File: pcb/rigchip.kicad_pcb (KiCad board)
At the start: 2 copper layers, 41 x 51 mm, 34 parts, among them IC1 TSR1, IC2 CHIPv1_0, IC3 SN74LVC1G07, IC4 SN74LVC1G07, J1 POWER, J2 DATA, J3 CONTROL

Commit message: more tweaking
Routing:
- net /PTT: track 20.2 -> 20.9 mm
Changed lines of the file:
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@@
   (general
     (links 73)
-    (no_connects 12)
-    (area 49.924999 48.924999 91.075001 100.075001)
+    (no_connects 0)
+    (area 48.794999 36.645 92.205001 101.625)
     (thickness 1.6)
     (drawings 18)
-    (tracks 349)
+    (tracks 345)
     (zones 0)
     (modules 34)
@@
   )
   (setup
-    (last_trace_width 0.3)
+    (last_trace_width 0.2)
     (user_trace_width 0.2)
     (user_trace_width 0.3)
@@
     (effects (font (size 1.5 1.5) (thickness 0.3)))
   )
+  (segment (start 63 57.46) (end 64.86 57.46) (width 0.3) (layer F.Cu) (net 1))
+  (segment (start 65.6 58.2) (end 65.6 71.1) (width 0.3) (layer F.Cu) (net 1))
+  (segment (start 65.6 71.1) (end 63.6 73.1) (width 0.3) (layer F.Cu) (net 1))
+  (segment (start 64.7 79.8) (end 65.5 79.8) (width 0.3) (layer F.Cu) (net 1))
+  (segment (start 64.86 57.46) (end 65.6 58.2) (width 0.3) (layer F.Cu) (net 1))
+  (segment (start 65.5 75) (end 65.8 75.3) (width 0.3) (layer F.Cu) (net 1))
+  (segment (start 63.6 73.1) (end 63.6 74.6) (width 0.3) (layer F.Cu) (net 1))
+  (segment (start 65.4 76.8) (end 64.8 76.8) (width 0.3) (layer F.Cu) (net 1))
+  (segment (start 63.6 74.6) (end 64 75) (width 0.3) (layer F.Cu) (net 1))
+  (segment (start 64 75) (end 65.5 75) (width 0.3) (layer F.Cu) (net 1))
+  (segment (start 65.8 75.3) (end 65.8 76.4) (width 0.3) (layer F.Cu) (net 1))
+  (segment (start 65.8 76.4) (end 65.4 76.8) (width 0.3) (layer F.Cu) (net 1))
+  (segment (start 64.8 76.8) (end 64.5 77.1) (width 0.3) (layer F.Cu) (net 1))
+  (segment (start 64.5 77.1) (end 64.5 79.6) (width 0.3) (layer F.Cu) (net 1))
+  (segment (start 64.5 79.6) (end 64.7 79.8) (width 0.3) (layer F.Cu) (net 1))
   (segment (start 65.5 79.8) (end 65.525 79.8) (width 0.2) (layer F.Cu) (net 1))
   (segment (start 66.349999 78.975001) (end 68.699999 78.975001) (width 0.2) (layer F.Cu) (net 1))
@@
   (segment (start 68.699999 78.975001) (end 69.475 78.2) (width 0.2) (layer F.Cu) (net 1))
   (segment (start 69.475 78.2) (end 69.5 78.2) (width 0.2) (layer F.Cu) (net 1))
-  (segment (start 64.86 57.46) (end 65.4 58) (width 0.3) (layer F.Cu) (net 1))
-  (segment (start 65.6 71.1) (end 65.6 58.2) (width 0.3) (layer F.Cu) (net 1))
-  (segment (start 64.5 77.1) (end 64.8 76.8) (width 0.3) (layer F.Cu) (net 1))
-  (segment (start 65.4 76.8) (end 65.8 76.4) (width 0.3) (layer F.Cu) (net 1))
-  (segment (start 65.5 79.8) (end 64.7 79.8) (width 0.3) (layer F.Cu) (net 1))
-  (segment (start 65.6 58.2) (end 65.4 58) (width 0.3) (layer F.Cu) (net 1))
-  (segment (start 64.7 79.8) (end 64.5 79.6) (width 0.3) (layer F.Cu) (net 1))
-  (segment (start 64.5 79.6) (end 64.5 77.1) (width 0.3) (layer F.Cu) (net 1))
-  (segment (start 64.8 76.8) (end 65.4 76.8) (width 0.3) (layer F.Cu) (net 1))
-  (segment (start 65.8 76.4) (end 65.8 75.2) (width 0.3) (layer F.Cu) (net 1))
-  (segment (start 65.8 75.2) (end 65.4 74.8) (width 0.3) (layer F.Cu) (net 1))
-  (segment (start 65.4 74.8) (end 63.8 74.8) (width 0.3) (layer F.Cu) (net 1))
-  (segment (start 63.8 74.8) (end 63.6 74.6) (width 0.3) (layer F.Cu) (net 1))
-  (segment (start 63.6 73.1) (end 65.6 71.1) (width 0.3) (layer F.Cu) (net 1))
-  (segment (start 63.6 74.6) (end 63.6 73.1) (width 0.3) (layer F.Cu) (net 1))
-  (segment (start 63 57.46) (end 64.86 57.46) (width 0.3) (layer F.Cu) (net 1))
   (segment (start 69.5 78.2) (end 69.5 76.15) (width 0.3) (layer F.Cu) (net 1))
   (segment (start 69.5 76.15) (end 69.7 75.95) (width 0.3) (layer F.Cu) (net 1))
@@
   (segment (start 80.475 76.05) (end 80.5 76.05) (width 0.2) (layer F.Cu) (net 5))
   (segment (start 80.5 78.2) (end 80.5 76.05) (width 0.3) (layer F.Cu) (net 5))
+  (segment (start 82.5 76.05) (end 81.8 76.05) (width 0.2) (layer F.Cu) (net 6))
+  (segment (start 81.8 76.05) (end 81.5 75.75) (width 0.2) (layer F.Cu) (net 6))
+  (segment (start 86.180009 64.860009) (end 87.03 65.71) (width 0.2) (layer F.Cu) (net 6))
+  (segment (start 81.5 75.75) (end 81.5 72.75) (width 0.2) (layer F.Cu) (net 6))
+  (segment (start 81.5 72.75) (end 81.25 72.5) (width 0.2) (layer F.Cu) (net 6))
+  (segment (start 81.25 72.5) (end 81.25 65.184998) (width 0.2) (layer F.Cu) (net 6))
+  (segment (start 81.25 65.184998) (end 81.574989 64.860009) (width 0.2) (layer F.Cu) (net 6))
+  (segment (start 81.574989 64.860009) (end 86.180009 64.860009) (width 0.2) (layer F.Cu) (net 6))
   (segment (start 87.03 65.71) (end 86.57 65.25) (width 0.2) (layer F.Cu) (net 6))
-  (segment (start 86.57 65.25) (end 85.5 65.25) (width 0.2) (layer F.Cu) (net 6))
-  (segment (start 85.5 65.25) (end 85.110009 64.860009) (width 0.2) (layer F.Cu) (net 6))
-  (segment (start 85.110009 64.860009) (end 81.574989 64.860009) (width 0.2) (layer F.Cu) (net 6))
-  (segment (start 81.574989 64.860009) (end 81.25 65.184998) (width 0.2) (layer F.Cu) (net 6))
-  (segment (start 81.25 65.184998) (end 81.25 72.5) (width 0.2) (layer F.Cu) (net 6))
-  (segment (start 81.25 72.5) (end 81.5 72.75) (width 0.2) (layer F.Cu) (net 6))
-  (segment (start 81.5 72.75) (end 81.5 75.75) (width 0.2) (layer F.Cu) (net 6))
-  (segment (start 81.5 75.75) (end 81.8 76.05) (width 0.2) (layer F.Cu) (net 6))
-  (segment (start 81.8 76.05) (end 82.5 76.05) (width 0.2) (layer F.Cu) (net 6))
   (segment (start 82.475 76.05) (end 82.5 76.05) (width 0.2) (layer F.Cu) (net 6))
   (segment (start 82.5 78.2) (end 82.5 76.05) (width 0.3) (layer F.Cu) (net 6))
@@
   (segment (start 87.03 55.55) (end 86.8 55.55) (width 0.3) (layer F.Cu) (net 81))
   (segment (start 86.98 55.5) (end 87.03 55.55) (width 0.3) (layer F.Cu) (net 81))
-  (segment (start 87.03 53.01) (end 76.99 53.01) (width 0.3) (layer F.Cu) (net 82))
-  (segment (start 76.99 53.01) (end 68.799999 61.200001) (width 0.3) (layer F.Cu) (net 82))
-  (segment (start 68.799999 61.200001) (end 68.799999 72.700001) (width 0.3) (layer F.Cu) (net 82))
-  (segment (start 68.799999 72.700001) (end 68.5 73) (width 0.3) (layer F.Cu) (net 82))
+  (segment (start 87.03 53.01) (end 76.24 53.01) (width 0.3) (layer F.Cu) (net 82))
+  (segment (start 76.24 53.01) (end 68.5 60.75) (width 0.3) (layer F.Cu) (net 82))
+  (segment (start 68.5 60.75) (end 68.5 74.65) (width 0.3) (layer F.Cu) (net 82))
+  (segment (start 68.5 74.65) (end 68.15 75) (width 0.3) (layer F.Cu) (net 82))
   (segment (start 68.15 75) (end 67.3 75) (width 0.3) (layer F.Cu) (net 82))
-  (segment (start 68.5 73) (end 68.5 74.65) (width 0.3) (layer F.Cu) (net 82))
-  (segment (start 68.5 74.65) (end 68.15 75) (width 0.3) (layer F.Cu) (net 82))
   (zone (net 2) (net_name GND) (layer B.Cu) (hatch edge 0.508)
     (connect_pads (clearance 0.3))

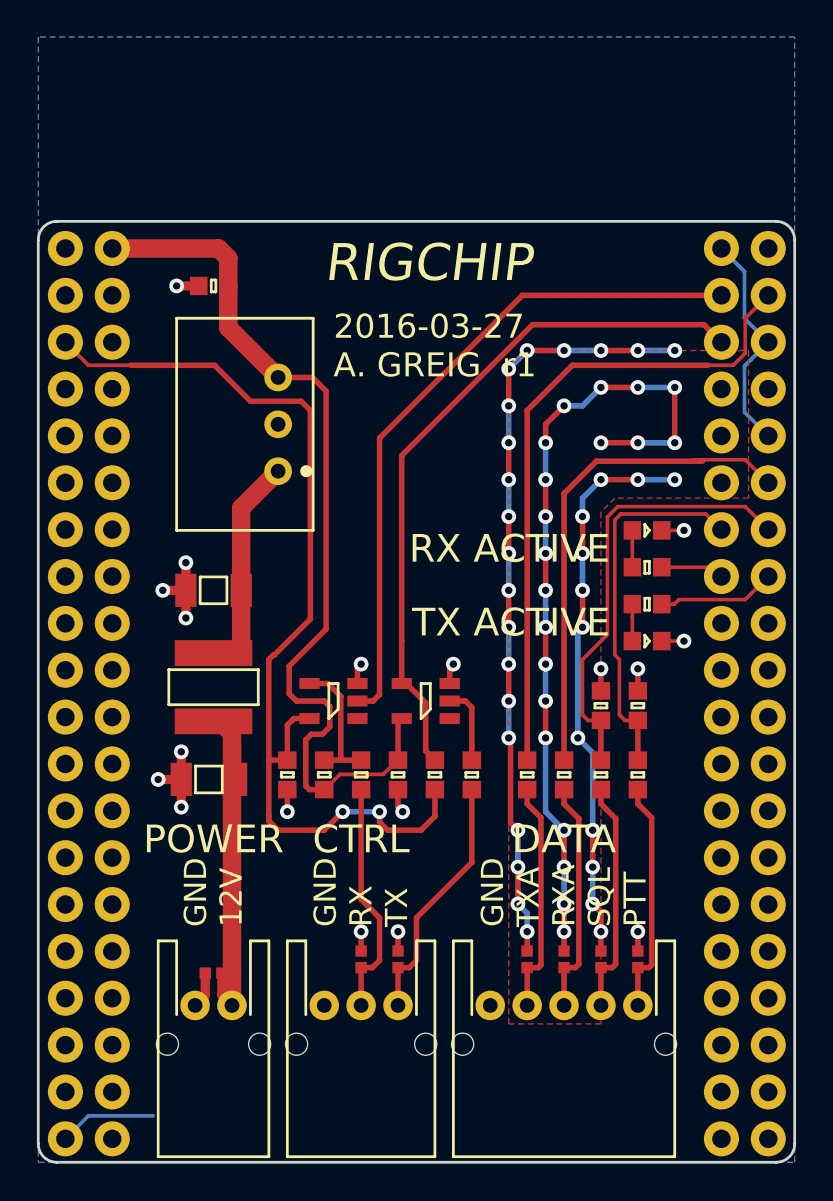
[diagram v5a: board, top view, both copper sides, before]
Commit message: LEDs to sink, driver on PTT, zener+R on SQL, reroute
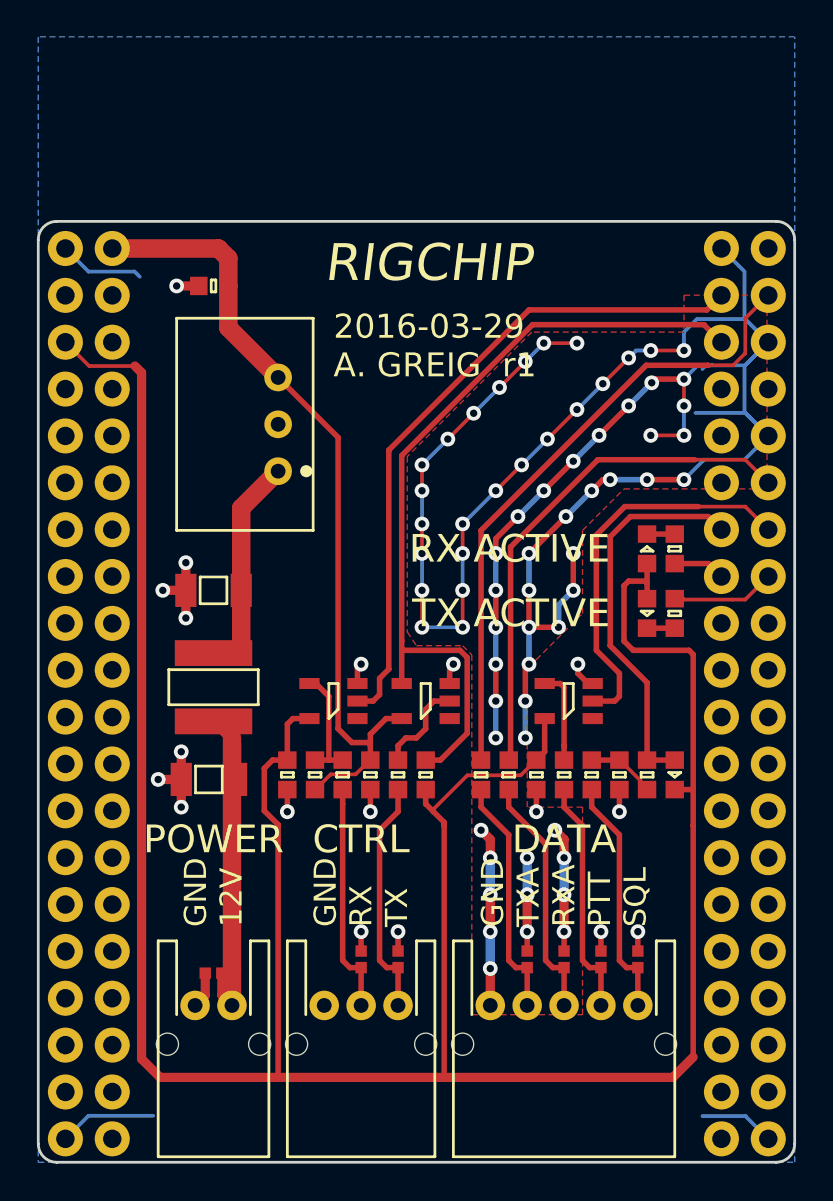
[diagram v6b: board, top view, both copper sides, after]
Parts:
- added D10: ~, agg:0603-LED, F.Cu at (84.5, 79.0)
- added IC5: SN74LVC1G07, agg:SOT-23-5, F.Cu at (78.8, 75.0)
- added R5: 10k, agg:0603, F.Cu at (83.0, 79.0)
- moved C5 6.66 mm to (77.0, 79.0), turned to 270 degrees
- moved L6 4.00 mm to (69.5, 79.0)
- moved C4 3.88 mm to (81.5, 79.0), turned to 270 degrees
- moved L4 3.00 mm to (75.5, 79.0)
- moved L2 2.50 mm to (80.0, 79.0)
- moved L5 2.50 mm to (74.0, 79.0)
- moved L3 2.00 mm to (78.5, 79.0)
- moved R1 1.80 mm to (84.5, 66.8), turned to 90 degrees
- moved R2 1.58 mm to (84.5, 70.2), turned to 270 degrees
- moved C7 1.50 mm to (68.0, 79.0)
- moved D9 1.50 mm to (83.0, 70.2), turned to 90 degrees
- moved D8 1.00 mm to (83.0, 66.8), turned to 270 degrees
- moved L7 1.00 mm to (66.5, 79.0)
- moved R3 0.50 mm to (65.0, 79.0)
- moved R4 0.50 mm to (71.0, 79.0)
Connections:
- C4 pad 1: /SQL -> Net-(C4-Pad1)
- C5 pad 1: /PTT -> 3v3
- D8 pad 1: GND -> Net-(D8-Pad1)
- D8 pad 2: Net-(D8-Pad2) -> 3v3
- D9 pad 1: GND -> Net-(D9-Pad1)
- D9 pad 2: Net-(D9-Pad2) -> 3v3
- IC2 pad L10: Net-(IC2-PadL10) -> (no net)
- IC2 pad L11: Net-(IC2-PadL11) -> (no net)
- IC2 pad L13: Net-(IC2-PadL13) -> (no net)
- IC2 pad L14: Net-(IC2-PadL14) -> (no net)
- IC2 pad L15: Net-(IC2-PadL15) -> (no net)
- IC2 pad L16: Net-(IC2-PadL16) -> (no net)
- IC2 pad L17: Net-(IC2-PadL17) -> (no net)
- IC2 pad L18: Net-(IC2-PadL18) -> (no net)
- IC2 pad L19: Net-(IC2-PadL19) -> (no net)
- IC2 pad L20: Net-(IC2-PadL20) -> (no net)
- IC2 pad L21: Net-(IC2-PadL21) -> (no net)
- IC2 pad L22: Net-(IC2-PadL22) -> (no net)
- IC2 pad L23: Net-(IC2-PadL23) -> (no net)
- IC2 pad L24: Net-(IC2-PadL24) -> (no net)
- IC2 pad L25: Net-(IC2-PadL25) -> (no net)
- IC2 pad L26: Net-(IC2-PadL26) -> (no net)
- IC2 pad L27: Net-(IC2-PadL27) -> (no net)
- IC2 pad L28: Net-(IC2-PadL28) -> (no net)
- IC2 pad L29: Net-(IC2-PadL29) -> (no net)
- IC2 pad L3: Net-(IC2-PadL3) -> (no net)
- IC2 pad L30: Net-(IC2-PadL30) -> (no net)
- IC2 pad L31: Net-(IC2-PadL31) -> (no net)
- IC2 pad L32: Net-(IC2-PadL32) -> (no net)
- IC2 pad L33: Net-(IC2-PadL33) -> (no net)
- IC2 pad L34: Net-(IC2-PadL34) -> (no net)
- IC2 pad L35: Net-(IC2-PadL35) -> (no net)
- IC2 pad L36: Net-(IC2-PadL36) -> (no net)
- IC2 pad L37: Net-(IC2-PadL37) -> (no net)
- IC2 pad L38: Net-(IC2-PadL38) -> (no net)
- IC2 pad L40: Net-(IC2-PadL40) -> (no net)
- IC2 pad L6: Net-(IC2-PadL6) -> (no net)
- IC2 pad L7: Net-(IC2-PadL7) -> (no net)
- IC2 pad L8: Net-(IC2-PadL8) -> (no net)
- IC2 pad L9: Net-(IC2-PadL9) -> (no net)
- IC2 pad R11: Net-(IC2-PadR11) -> (no net)
- IC2 pad R13: /PTT -> /SQL
- IC2 pad R14: /SQL -> /CHIP_PTT
- IC2 pad R17: Net-(IC2-PadR17) -> (no net)
- IC2 pad R18: Net-(IC2-PadR18) -> (no net)
- IC2 pad R19: Net-(IC2-PadR19) -> (no net)
- IC2 pad R2: Net-(IC2-PadR2) -> (no net)
- IC2 pad R20: Net-(IC2-PadR20) -> (no net)
- IC2 pad R23: Net-(IC2-PadR23) -> (no net)
- IC2 pad R24: Net-(IC2-PadR24) -> (no net)
- IC2 pad R25: Net-(IC2-PadR25) -> (no net)
- IC2 pad R26: Net-(IC2-PadR26) -> (no net)
- IC2 pad R27: Net-(IC2-PadR27) -> (no net)
- IC2 pad R28: Net-(IC2-PadR28) -> (no net)
- IC2 pad R29: Net-(IC2-PadR29) -> (no net)
- IC2 pad R30: Net-(IC2-PadR30) -> (no net)
- IC2 pad R31: Net-(IC2-PadR31) -> (no net)
- IC2 pad R32: Net-(IC2-PadR32) -> (no net)
- IC2 pad R33: Net-(IC2-PadR33) -> (no net)
- IC2 pad R34: Net-(IC2-PadR34) -> (no net)
- IC2 pad R35: Net-(IC2-PadR35) -> (no net)
- IC2 pad R36: Net-(IC2-PadR36) -> (no net)
- IC2 pad R37: Net-(IC2-PadR37) -> (no net)
- IC2 pad R38: Net-(IC2-PadR38) -> (no net)
- IC2 pad R7: Net-(IC2-PadR7) -> (no net)
- IC2 pad R8: Net-(IC2-PadR8) -> (no net)
- IC2 pad R9: Net-(IC2-PadR9) -> (no net)
- IC3 pad 1: Net-(IC3-Pad1) -> (no net)
- IC4 pad 1: Net-(IC4-Pad1) -> (no net)
- L2 pad 2: /PTT -> Net-(C4-Pad1)
- L3 pad 2: /SQL -> /RIG_PTT
- R1 pad 2: Net-(D8-Pad2) -> Net-(D8-Pad1)
- R2 pad 2: Net-(D9-Pad2) -> Net-(D9-Pad1)
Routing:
- net 3v3: track 54.4 -> 153.0 mm, vias 2 -> 0
- net GND: track 157.7 -> 193.9 mm, vias 70 -> 84
- net /CHIP_PTT: track 0.00 -> 21.3 mm
- net /PTT: track 20.9 -> 0.00 mm
- net 5v: track 50.0 -> 43.6 mm
- net /CHIP_RX: track 38.4 -> 44.2 mm
- net /RIG_PTT: track 0.00 -> 5.33 mm
- net Net-(C4-Pad1): track 0.00 -> 3.74 mm
- net /SQL: track 24.1 -> 21.2 mm
- net Net-(D9-Pad2): track 2.00 -> 0.00 mm
- net Net-(D8-Pad2): track 2.00 -> 0.00 mm
- net Net-(D9-Pad1): track 0.00 -> 1.50 mm
- net Net-(D8-Pad1): track 0.00 -> 1.50 mm
- net /TX_AUDIO: track 35.7 -> 34.4 mm
- net /RIG_TX: track 4.19 -> 5.19 mm
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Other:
- board text added: "2016-03-29 A. GREIG r1"
- board text added: "GND TXA RXA PTT SQL"
- board text removed: "2016-03-27 A. GREIG r1"
- board text removed: "GND TXA RXA SQL PTT"
